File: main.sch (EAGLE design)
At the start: 49 parts, among them IC1 MEGA8-AI, IC2 MCP73831, IC3 7805DT, Q2 32768k

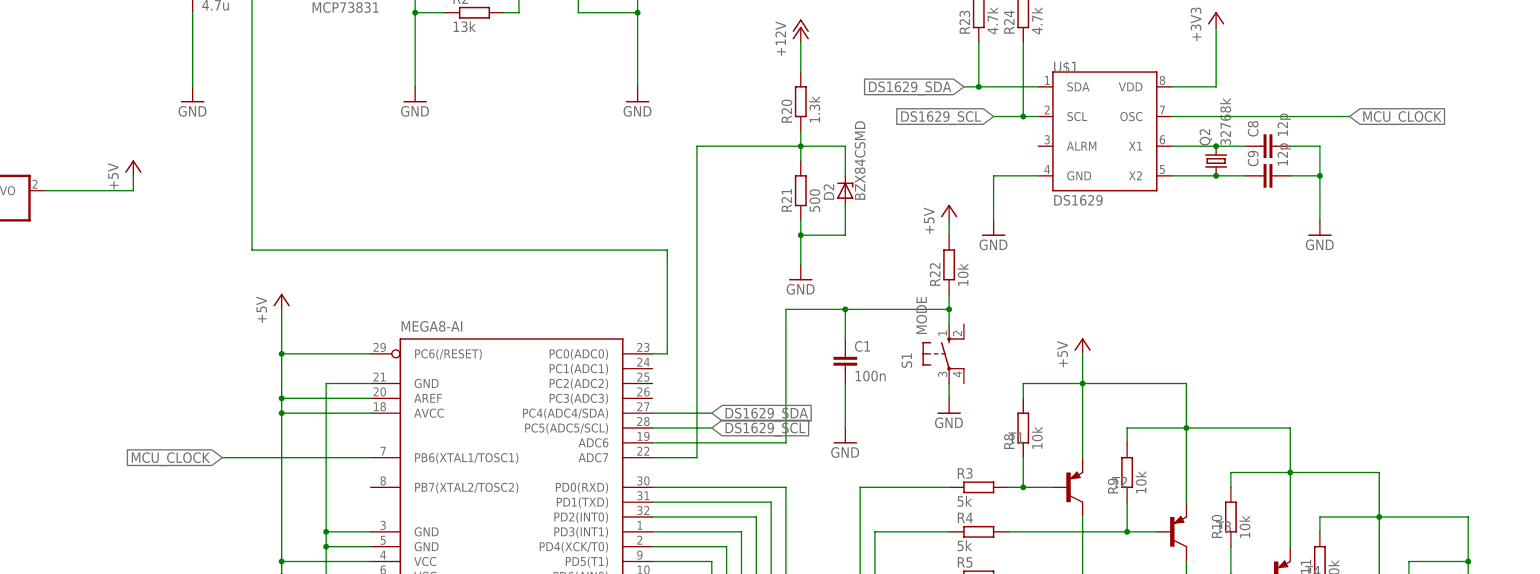
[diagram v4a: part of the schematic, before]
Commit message: Remove MCU external clock, use internal RC 4 MHz
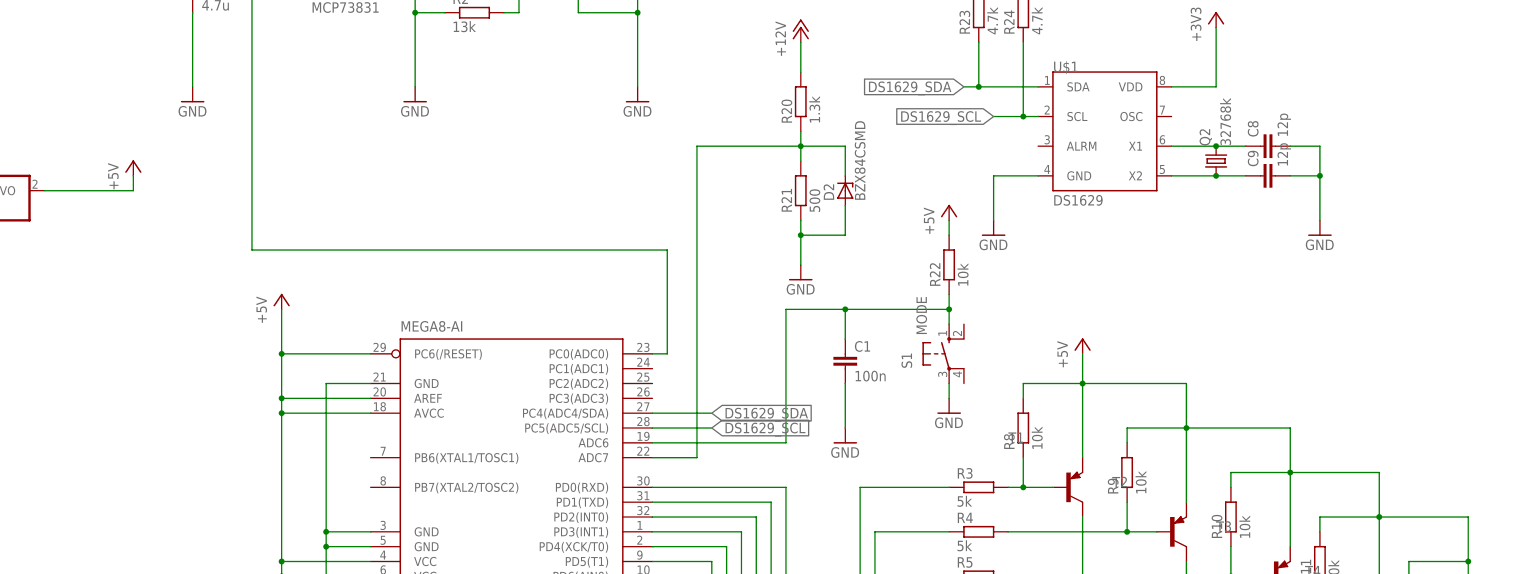
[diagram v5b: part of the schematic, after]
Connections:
- removed net MCU_CLOCK: IC1.PB6(XTAL1/TOSC1), U$1.OSC
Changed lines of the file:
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@@
-</segment>
-</net>
-<net name="MCU_CLOCK" class="0">
-<segment>
-<wire x1="144.78" y1="134.62" x2="119.38" y2="134.62" width="0.1524" layer="91"/>
-<label x="119.38" y="134.62" size="1.778" layer="95" rot="R180" xref="yes"/>
-<pinref part="IC1" gate="G$1" pin="PB6(XTAL1/TOSC1)"/>
-</segment>
-<segment>
-<pinref part="U$1" gate="G$1" pin="OSC"/>
-<wire x1="281.94" y1="193.04" x2="312.42" y2="193.04" width="0.1524" layer="91"/>
-<label x="312.42" y="193.04" size="1.778" layer="95" xref="yes"/>
 </segment>
 </net>

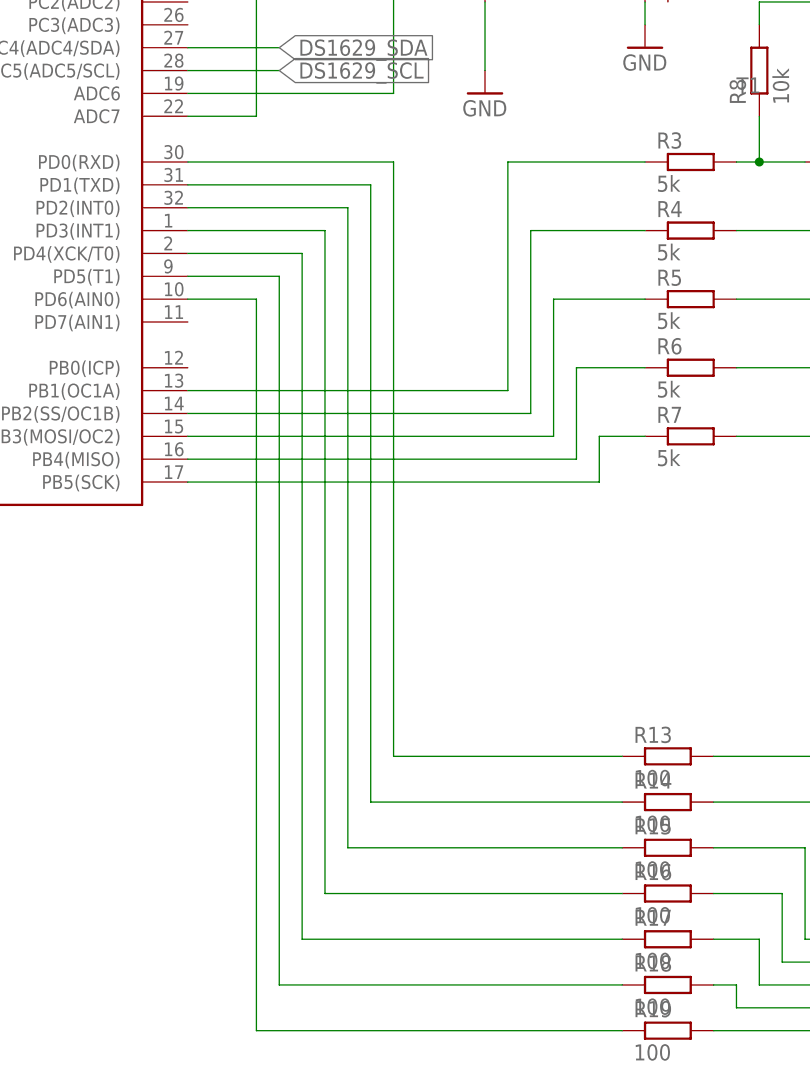
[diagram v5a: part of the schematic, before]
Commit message: Move display pins to make debug pin
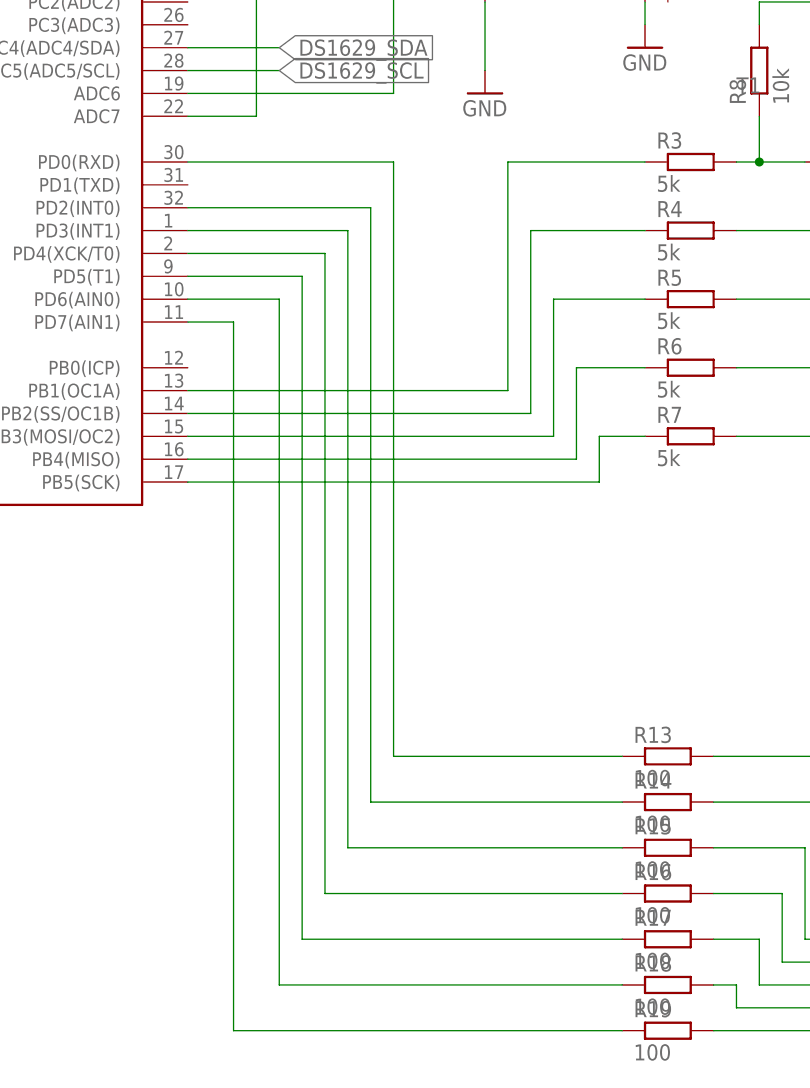
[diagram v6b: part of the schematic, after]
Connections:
- net N$19: now also IC1.PD5(T1); no longer IC1.PD4(XCK/T0)
- net N$21: now also IC1.PD2(INT0); no longer IC1.PD1(TXD)
- net N$22: now also IC1.PD3(INT1); no longer IC1.PD2(INT0)
- net N$30: now also IC1.PD4(XCK/T0); no longer IC1.PD3(INT1)
- net N$35: now also IC1.PD6(AIN0); no longer IC1.PD5(T1)
- net N$36: now also IC1.PD7(AIN1); no longer IC1.PD6(AIN0)
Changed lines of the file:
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@@
 <segment>
 <pinref part="R13" gate="G$1" pin="1"/>
-<wire x1="215.9" y1="129.54" x2="215.9" y2="63.5" width="0.1524" layer="91"/>
 <wire x1="215.9" y1="63.5" x2="241.3" y2="63.5" width="0.1524" layer="91"/>
+<wire x1="215.9" y1="63.5" x2="215.9" y2="129.54" width="0.1524" layer="91"/>
 <pinref part="IC1" gate="G$1" pin="PD0(RXD)"/>
-<wire x1="193.04" y1="129.54" x2="215.9" y2="129.54" width="0.1524" layer="91"/>
+<wire x1="215.9" y1="129.54" x2="193.04" y2="129.54" width="0.1524" layer="91"/>
 </segment>
 </net>
@@
 <segment>
 <pinref part="R14" gate="G$1" pin="1"/>
-<wire x1="213.36" y1="127" x2="213.36" y2="58.42" width="0.1524" layer="91"/>
 <wire x1="213.36" y1="58.42" x2="241.3" y2="58.42" width="0.1524" layer="91"/>
-<pinref part="IC1" gate="G$1" pin="PD1(TXD)"/>
-<wire x1="193.04" y1="127" x2="213.36" y2="127" width="0.1524" layer="91"/>
+<wire x1="213.36" y1="58.42" x2="213.36" y2="124.46" width="0.1524" layer="91"/>
+<pinref part="IC1" gate="G$1" pin="PD2(INT0)"/>
+<wire x1="213.36" y1="124.46" x2="193.04" y2="124.46" width="0.1524" layer="91"/>
 </segment>
 </net>
@@
 <segment>
 <pinref part="R15" gate="G$1" pin="1"/>
-<wire x1="210.82" y1="124.46" x2="210.82" y2="53.34" width="0.1524" layer="91"/>
 <wire x1="210.82" y1="53.34" x2="241.3" y2="53.34" width="0.1524" layer="91"/>
-<pinref part="IC1" gate="G$1" pin="PD2(INT0)"/>
-<wire x1="193.04" y1="124.46" x2="210.82" y2="124.46" width="0.1524" layer="91"/>
+<wire x1="210.82" y1="53.34" x2="210.82" y2="121.92" width="0.1524" layer="91"/>
+<pinref part="IC1" gate="G$1" pin="PD3(INT1)"/>
+<wire x1="210.82" y1="121.92" x2="193.04" y2="121.92" width="0.1524" layer="91"/>
 </segment>
 </net>
@@
 <segment>
 <pinref part="R16" gate="G$1" pin="1"/>
-<wire x1="208.28" y1="121.92" x2="208.28" y2="48.26" width="0.1524" layer="91"/>
 <wire x1="208.28" y1="48.26" x2="241.3" y2="48.26" width="0.1524" layer="91"/>
-<pinref part="IC1" gate="G$1" pin="PD3(INT1)"/>
-<wire x1="193.04" y1="121.92" x2="208.28" y2="121.92" width="0.1524" layer="91"/>
+<wire x1="208.28" y1="48.26" x2="208.28" y2="119.38" width="0.1524" layer="91"/>
+<pinref part="IC1" gate="G$1" pin="PD4(XCK/T0)"/>
+<wire x1="208.28" y1="119.38" x2="193.04" y2="119.38" width="0.1524" layer="91"/>
 </segment>
 </net>
@@
 <segment>
 <pinref part="R17" gate="G$1" pin="1"/>
-<wire x1="205.74" y1="119.38" x2="205.74" y2="43.18" width="0.1524" layer="91"/>
 <wire x1="205.74" y1="43.18" x2="241.3" y2="43.18" width="0.1524" layer="91"/>
-<pinref part="IC1" gate="G$1" pin="PD4(XCK/T0)"/>
-<wire x1="193.04" y1="119.38" x2="205.74" y2="119.38" width="0.1524" layer="91"/>
+<wire x1="205.74" y1="43.18" x2="205.74" y2="116.84" width="0.1524" layer="91"/>
+<pinref part="IC1" gate="G$1" pin="PD5(T1)"/>
+<wire x1="205.74" y1="116.84" x2="193.04" y2="116.84" width="0.1524" layer="91"/>
 </segment>
 </net>
@@
 <segment>
 <pinref part="R18" gate="G$1" pin="1"/>
-<wire x1="203.2" y1="116.84" x2="203.2" y2="38.1" width="0.1524" layer="91"/>
 <wire x1="203.2" y1="38.1" x2="241.3" y2="38.1" width="0.1524" layer="91"/>
-<pinref part="IC1" gate="G$1" pin="PD5(T1)"/>
-<wire x1="193.04" y1="116.84" x2="203.2" y2="116.84" width="0.1524" layer="91"/>
+<wire x1="203.2" y1="38.1" x2="203.2" y2="114.3" width="0.1524" layer="91"/>
+<pinref part="IC1" gate="G$1" pin="PD6(AIN0)"/>
+<wire x1="203.2" y1="114.3" x2="193.04" y2="114.3" width="0.1524" layer="91"/>
 </segment>
 </net>
@@
 <segment>
 <pinref part="R19" gate="G$1" pin="1"/>
-<wire x1="200.66" y1="114.3" x2="200.66" y2="33.02" width="0.1524" layer="91"/>
-<wire x1="200.66" y1="33.02" x2="241.3" y2="33.02" width="0.1524" layer="91"/>
-<pinref part="IC1" gate="G$1" pin="PD6(AIN0)"/>
-<wire x1="193.04" y1="114.3" x2="200.66" y2="114.3" width="0.1524" layer="91"/>
+<wire x1="198.12" y1="33.02" x2="241.3" y2="33.02" width="0.1524" layer="91"/>
+<wire x1="198.12" y1="33.02" x2="198.12" y2="111.76" width="0.1524" layer="91"/>
+<pinref part="IC1" gate="G$1" pin="PD7(AIN1)"/>
+<wire x1="198.12" y1="111.76" x2="193.04" y2="111.76" width="0.1524" layer="91"/>
 </segment>
 </net>

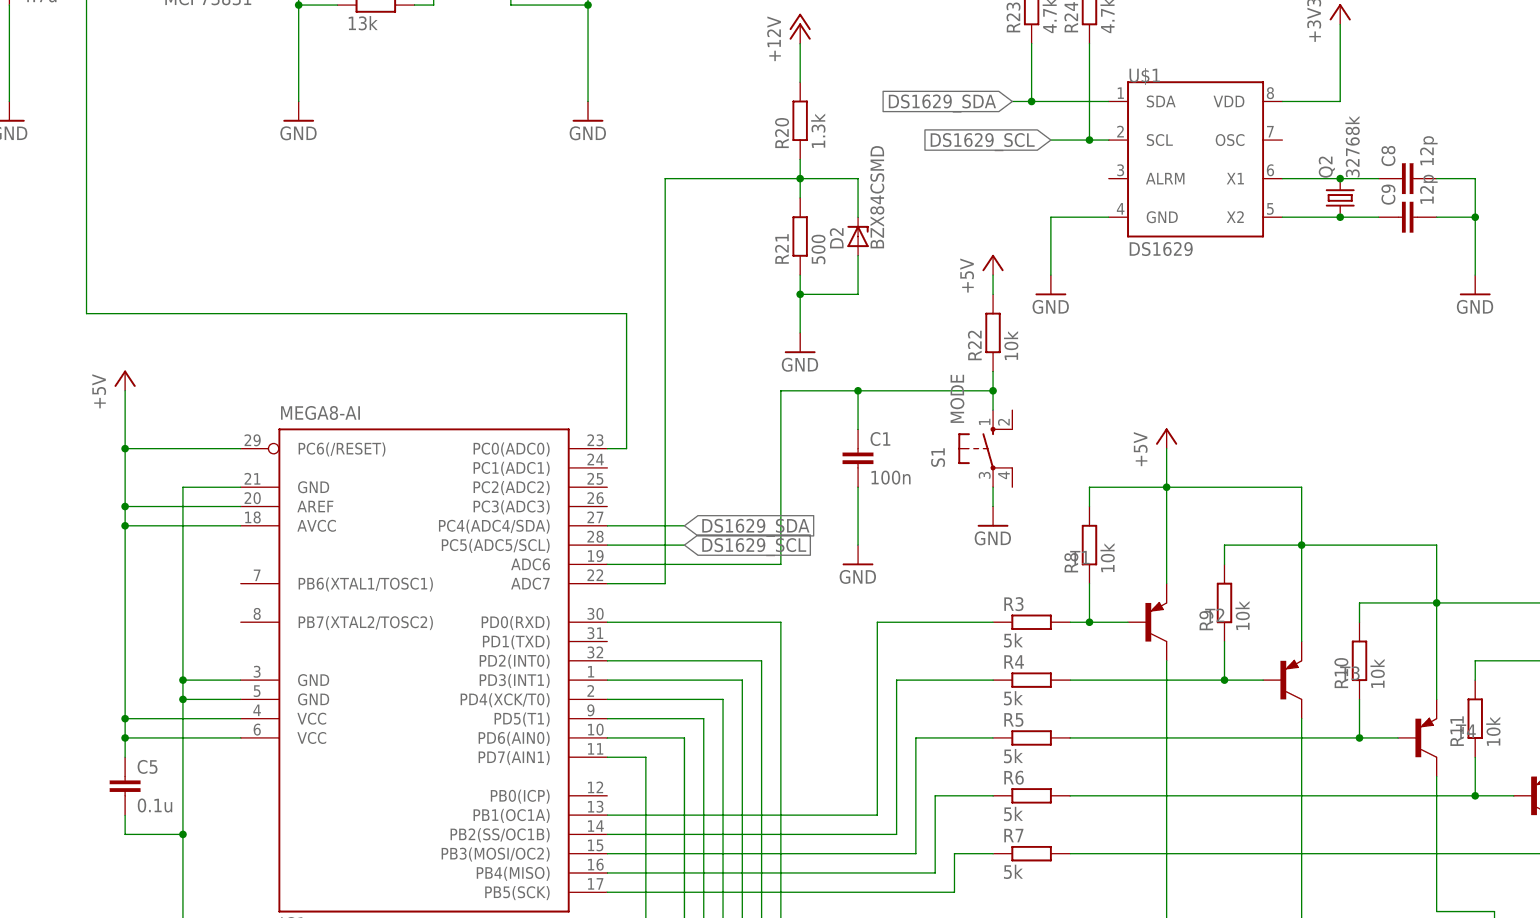
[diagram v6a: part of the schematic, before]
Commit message: Change resistors/capacitors packages from 1206 to 0805
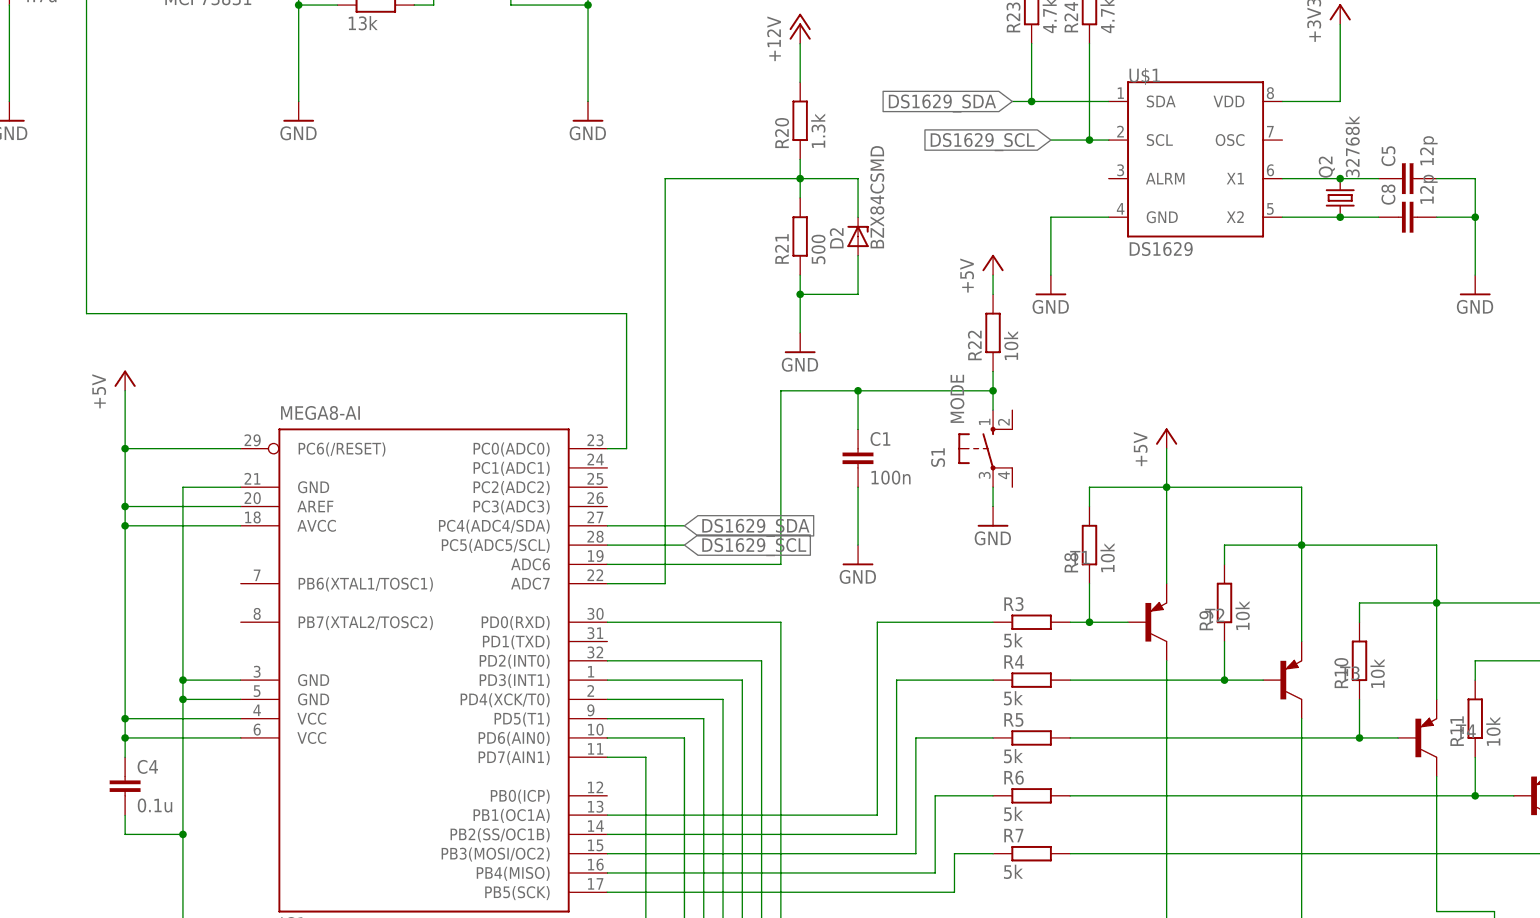
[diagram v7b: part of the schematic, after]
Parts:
- removed C9: 12p, rcl:C-EUC1206
- added C4: 0.1u, rcl:C-EUC0805
- C1, C8: device rcl:C-EUC1206 -> rcl:C-EUC0805
- C5: value 0.1u -> 12p; device rcl:C-EUC1206 -> rcl:C-EUC0805
- R1: device rcl:R-EU_M1206 -> rcl:R-EU_M0805
- R10, R11, R12, R13, R14, R15, R16, R17, R18, R19, R2, R20, R21, R22, R23, R24, R3, R4, R5, R6, R7, R8, R9: device rcl:R-EU_R1206 -> rcl:R-EU_M0805
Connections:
- net +5V: now also C4.1; no longer C5.1
- net GND: now also C4.2; no longer C9.2
- net N$28: now also C5.1; no longer C8.1
- net N$29: now also C8.1; no longer C9.1
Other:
- moved on the sheet: C5, C8

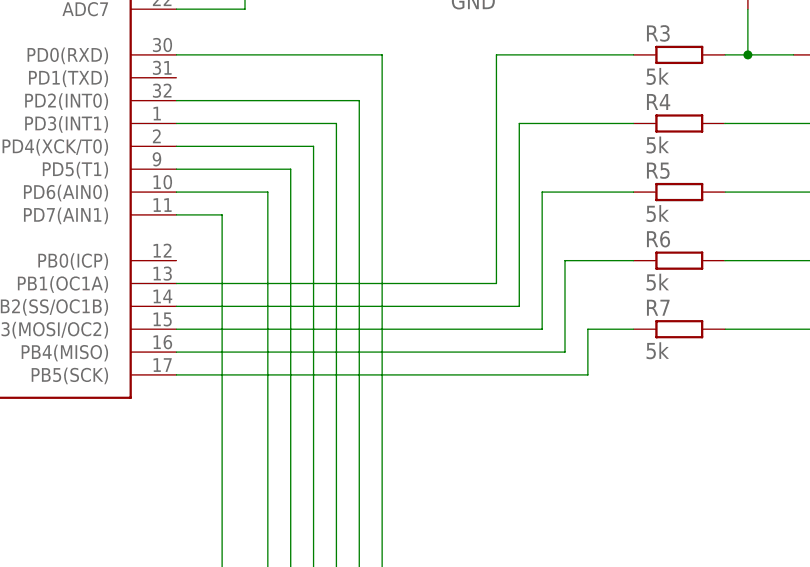
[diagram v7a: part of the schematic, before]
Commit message: Swap PB3<=>PB5
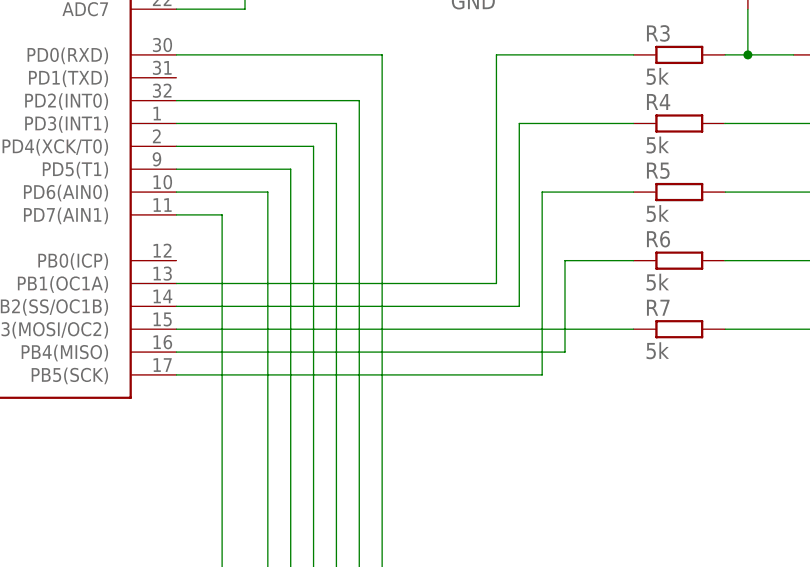
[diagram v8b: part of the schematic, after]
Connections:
- net N$25: now also IC1.PB5(SCK); no longer IC1.PB3(MOSI/OC2)
- net N$27: now also IC1.PB3(MOSI/OC2); no longer IC1.PB5(SCK)
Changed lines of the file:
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@@
 <net name="N$25" class="0">
 <segment>
-<wire x1="193.04" y1="99.06" x2="233.68" y2="99.06" width="0.1524" layer="91"/>
-<wire x1="233.68" y1="99.06" x2="233.68" y2="114.3" width="0.1524" layer="91"/>
+<wire x1="233.68" y1="93.98" x2="233.68" y2="114.3" width="0.1524" layer="91"/>
 <wire x1="233.68" y1="114.3" x2="243.84" y2="114.3" width="0.1524" layer="91"/>
-<pinref part="IC1" gate="G$1" pin="PB3(MOSI/OC2)"/>
 <pinref part="R5" gate="G$1" pin="1"/>
+<pinref part="IC1" gate="G$1" pin="PB5(SCK)"/>
+<wire x1="233.68" y1="93.98" x2="193.04" y2="93.98" width="0.1524" layer="91"/>
 </segment>
 </net>
@@
 <net name="N$27" class="0">
 <segment>
-<wire x1="243.84" y1="99.06" x2="238.76" y2="99.06" width="0.1524" layer="91"/>
-<wire x1="238.76" y1="99.06" x2="238.76" y2="93.98" width="0.1524" layer="91"/>
-<wire x1="238.76" y1="93.98" x2="193.04" y2="93.98" width="0.1524" layer="91"/>
-<pinref part="IC1" gate="G$1" pin="PB5(SCK)"/>
 <pinref part="R7" gate="G$1" pin="1"/>
+<pinref part="IC1" gate="G$1" pin="PB3(MOSI/OC2)"/>
+<wire x1="243.84" y1="99.06" x2="193.04" y2="99.06" width="0.1524" layer="91"/>
 </segment>
 </net>
